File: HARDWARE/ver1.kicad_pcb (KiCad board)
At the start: 2 copper layers, 136.3 x 108.3 mm, 7 parts

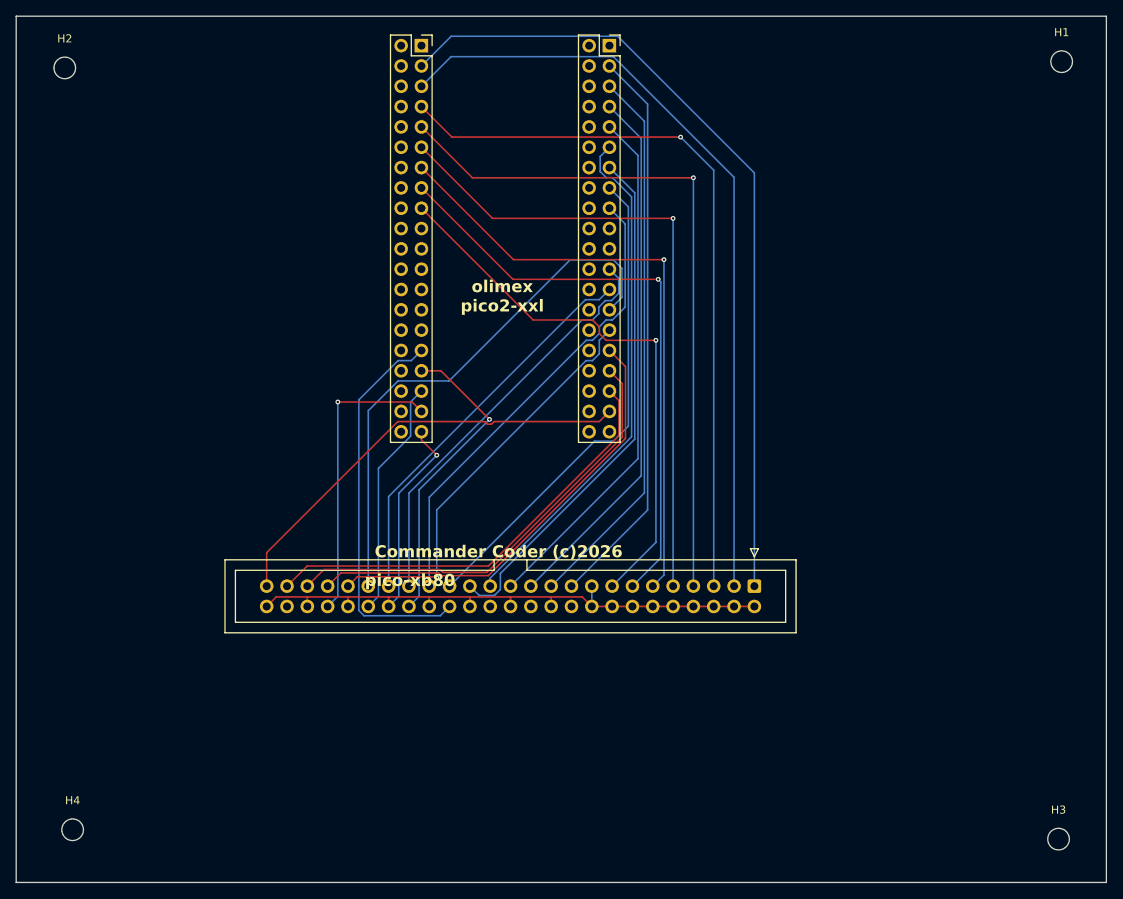
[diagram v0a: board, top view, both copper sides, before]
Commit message: adding output for HARDWARE
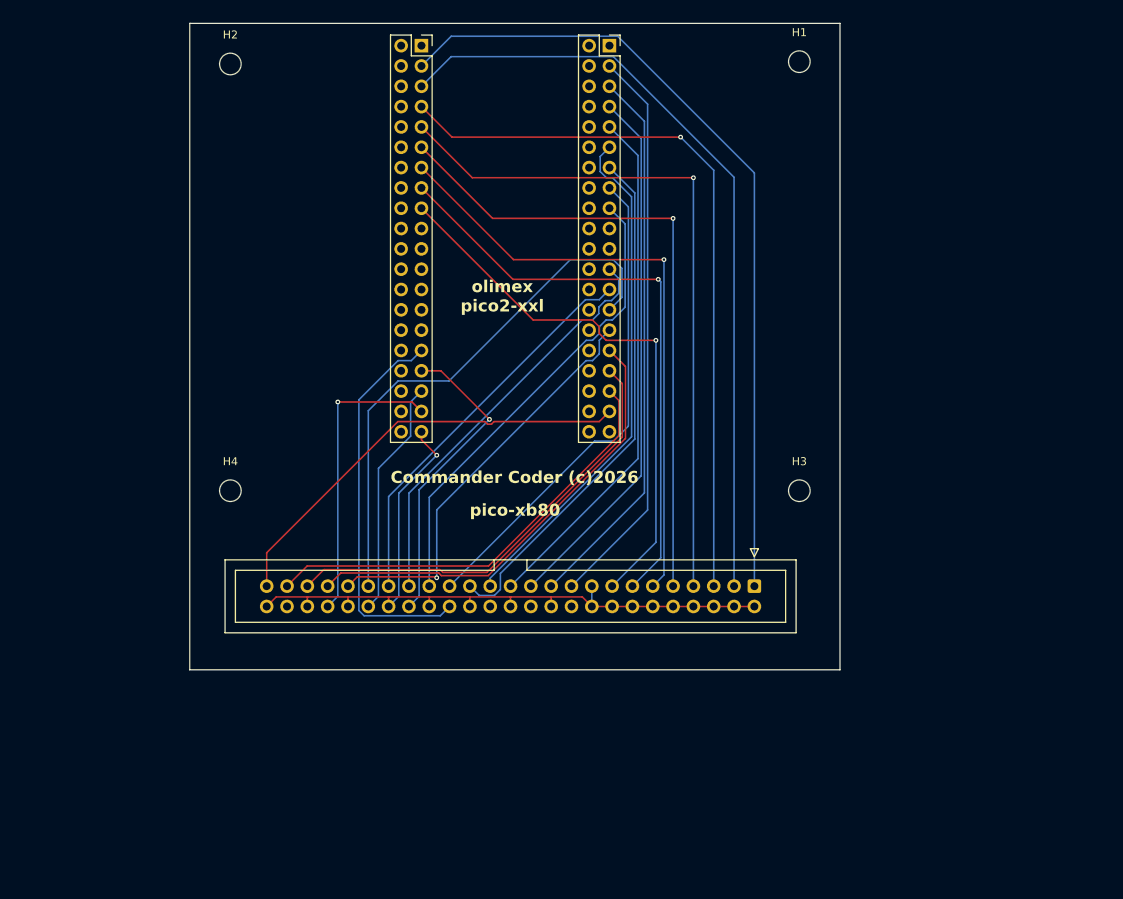
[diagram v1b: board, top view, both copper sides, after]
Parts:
- moved H3 54.3 mm to (149.9, 116.8)
- moved H4 46.7 mm to (78.7, 116.8)
- moved H1 32.8 mm to (149.9, 63.2)
- moved H2 20.7 mm to (78.7, 63.5)
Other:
- board size 136.3 x 108.3 mm -> 81.3 x 80.8 mm
